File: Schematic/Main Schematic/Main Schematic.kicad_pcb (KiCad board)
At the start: 2 copper layers, 48 parts, among them IC1 DW01A-G, IC2 LM75AD,118, J1 Conn_01x24_Socket, J10 Conn_01x08_Pin, J3 Conn_01x24_Socket, J4 Conn_01x02_Male, J5 Conn_01x02_Male, J6 USB_B_Micro, J7 Conn_01x02_Pin, J8 Conn_01x24_Pin, J9 Conn_01x24_Pin, Q1 FS8205A, SW1 SW_Push, U1 HT75xx-1-SOT89, U2 MCP73831-2-OT, U3 CH340C, U4 M24C16-RMN6TP

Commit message: PCB UPDATE
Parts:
- moved TP7 109.6 mm to (106.4, 100.4)
- moved TP6 107.6 mm to (106.6, 105.0)
- moved J7 94.0 mm to (100.6, 107.3)
- moved J4 79.6 mm to (182.5, 79.5)
- moved U4 73.9 mm to (181.6, 130.4), turned to -90 degrees
- moved C7 73.0 mm to (126.8, 99.2), turned to -90 degrees
- moved J5 68.0 mm to (175.5, 79.5)
- moved U1 61.5 mm to (180.9, 94.0)
- moved J8 58.8 mm to (111.7, 119.4), turned to 90 degrees
- moved J9 56.8 mm to (111.7, 145.7), turned to 90 degrees
- moved J3 54.6 mm to (111.7, 124.5), turned to 90 degrees
- moved J1 53.5 mm to (111.7, 141.0), turned to 90 degrees
- moved IC2 52.8 mm to (159.0, 108.0), turned to -90 degrees
- moved TP2 50.6 mm to (132.0, 105.0)
- moved C2 50.1 mm to (175.9, 99.5), turned to -90 degrees
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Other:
- board outline added: 100 x 100 mm

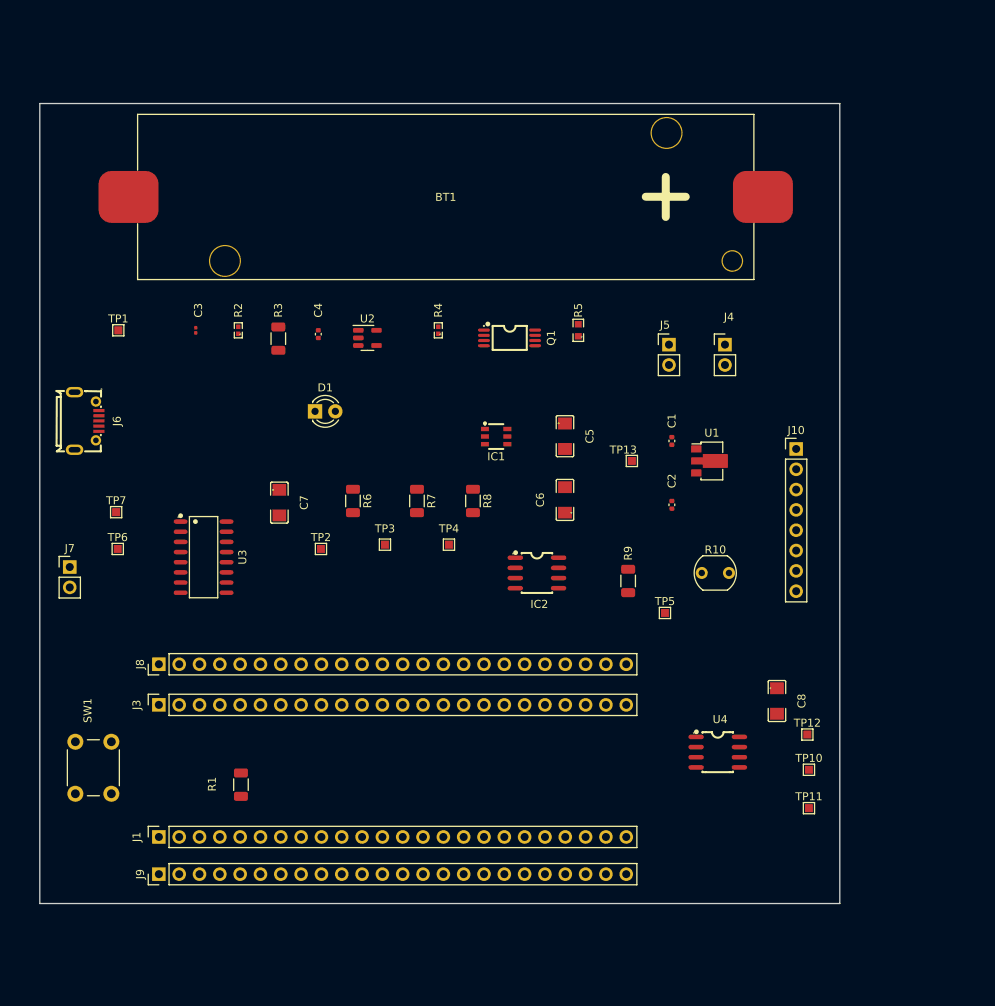
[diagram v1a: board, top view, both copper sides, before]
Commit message: traces done
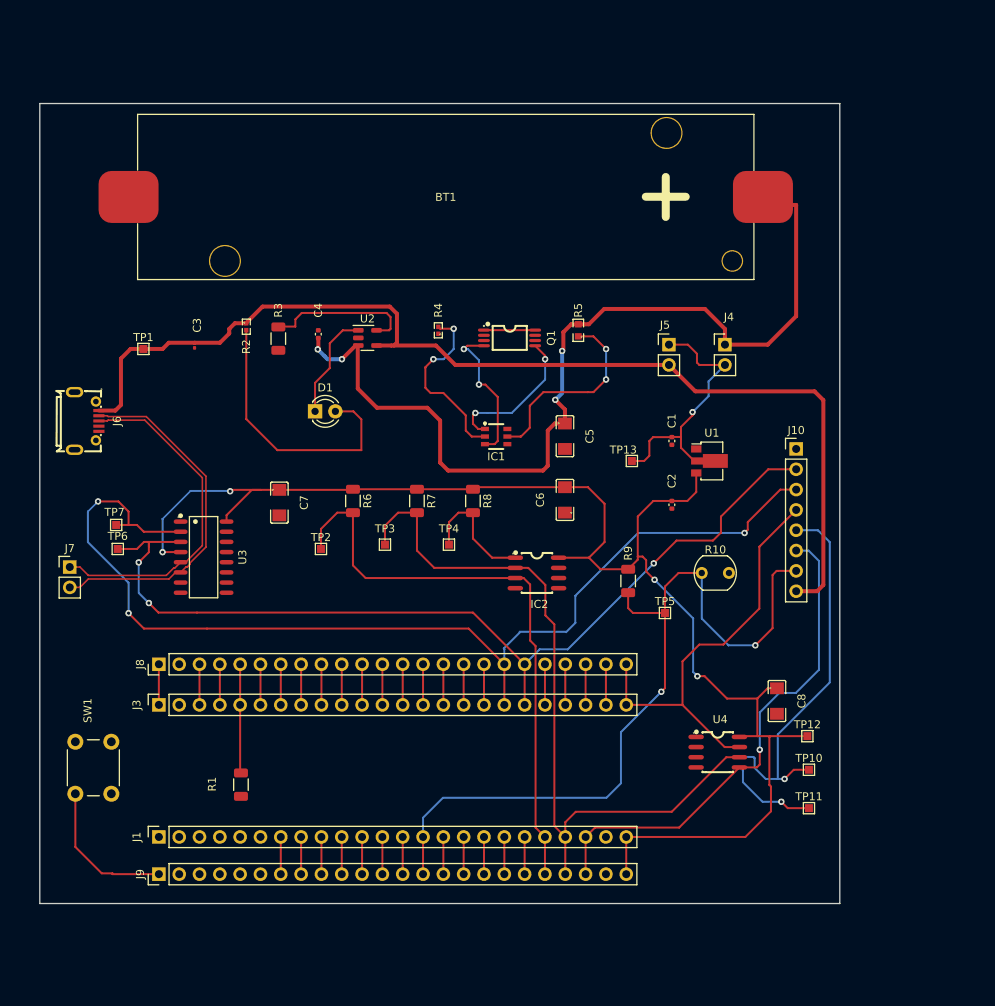
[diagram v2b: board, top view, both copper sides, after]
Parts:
- moved TP1 3.90 mm to (109.8, 80.0)
- moved C3 1.88 mm to (116.2, 79.5)
- moved TP7 1.60 mm to (106.4, 102.0)
- moved R2 1.10 mm to (122.7, 77.2), turned to -90 degrees
- moved TP12 0.20 mm to (192.8, 128.4)
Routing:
- net /3.3V: track 0.00 -> 192.1 mm, vias 0 -> 4
- net /SCL: track 0.00 -> 142.9 mm, vias 0 -> 1
- net /5V: track 0.00 -> 136.7 mm
- net /TXD: track 0.00 -> 135.1 mm, vias 0 -> 3
- net /RXD: track 0.00 -> 118.0 mm, vias 0 -> 3
- net /Power Unit/V1: track 0.00 -> 117.0 mm, vias 0 -> 4
- net /ADC: track 0.00 -> 99.4 mm, vias 0 -> 2
- net /SDL: track 0.00 -> 90.7 mm, vias 0 -> 2
- net /OS: track 0.00 -> 74.0 mm
- net /WRITE: track 0.00 -> 53.4 mm
- net /USB D-: track 0.00 -> 44.6 mm
- net /USB D+: track 0.00 -> 43.0 mm
- net Net-(D1-A): track 0.00 -> 34.6 mm
- net Net-(#FLG02-pwr): track 0.00 -> 32.6 mm, vias 0 -> 1
- net Net-(IC1-VCC): track 0.00 -> 24.8 mm, vias 0 -> 2
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
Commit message: updated the conn connections
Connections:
- J9 pad 2: /PF1 -> /PC13
- J9 pad 3: /PF0 -> /PC14
- J9 pad 5: /PC14 -> /PF0
- J9 pad 6: /PC13 -> /PF1
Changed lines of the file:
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@@
       (net 21 "/NRST") (pinfunction "Pin_1") (pintype "passive"))
     (pad "2" thru_hole oval (at 0 2.54 90) (size 1.7 1.7) (drill 1) (layers "*.Cu" "*.Mask")
-      (net 20 "/PF1") (pinfunction "Pin_2") (pintype "passive"))
+      (net 16 "/PC13") (pinfunction "Pin_2") (pintype "passive"))
     (pad "3" thru_hole oval (at 0 5.08 90) (size 1.7 1.7) (drill 1) (layers "*.Cu" "*.Mask")
-      (net 19 "/PF0") (pinfunction "Pin_3") (pintype "passive"))
+      (net 17 "/PC14") (pinfunction "Pin_3") (pintype "passive"))
     (pad "4" thru_hole oval (at 0 7.62 90) (size 1.7 1.7) (drill 1) (layers "*.Cu" "*.Mask")
       (net 18 "/PC15") (pinfunction "Pin_4") (pintype "passive"))
     (pad "5" thru_hole oval (at 0 10.16 90) (size 1.7 1.7) (drill 1) (layers "*.Cu" "*.Mask")
-      (net 17 "/PC14") (pinfunction "Pin_5") (pintype "passive"))
+      (net 19 "/PF0") (pinfunction "Pin_5") (pintype "passive"))
     (pad "6" thru_hole oval (at 0 12.7 90) (size 1.7 1.7) (drill 1) (layers "*.Cu" "*.Mask")
-      (net 16 "/PC13") (pinfunction "Pin_6") (pintype "passive"))
+      (net 20 "/PF1") (pinfunction "Pin_6") (pintype "passive"))
     (pad "7" thru_hole oval (at 0 15.24 90) (size 1.7 1.7) (drill 1) (layers "*.Cu" "*.Mask")
       (net 21 "/NRST") (pinfunction "Pin_7") (pintype "passive"))

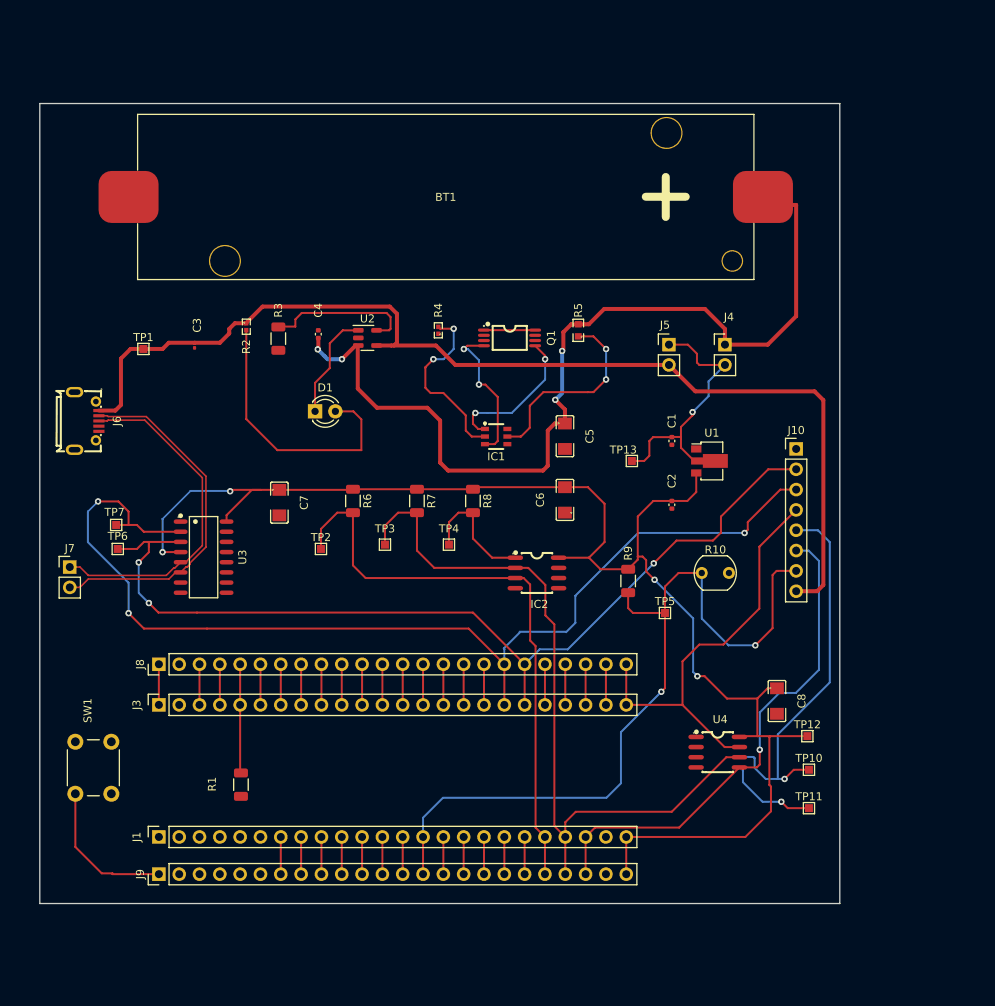
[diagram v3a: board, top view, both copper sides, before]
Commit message: traces done
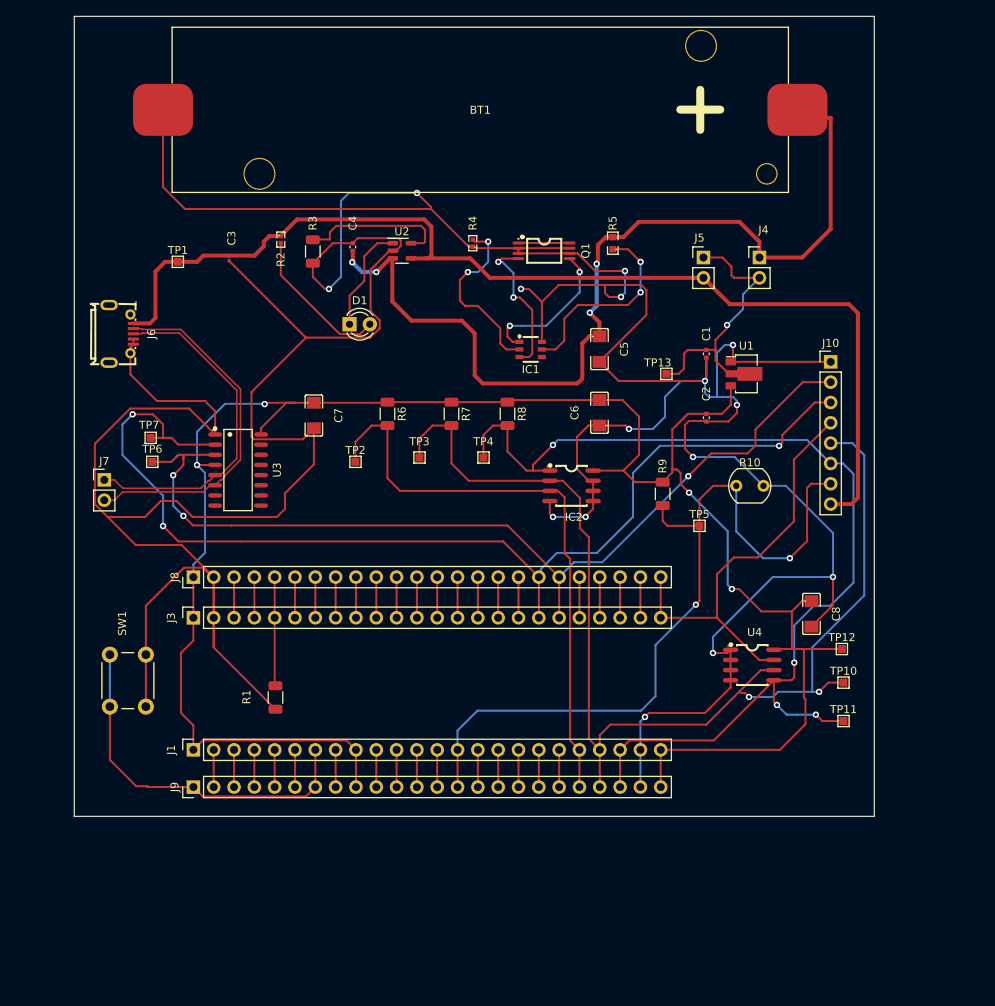
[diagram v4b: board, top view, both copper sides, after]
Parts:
- moved C4 11.7 mm to (136.0, 67.3)
- moved R4 11.7 mm to (151.0, 66.8)
- moved R5 11.7 mm to (168.5, 66.8)
- moved C7 11.7 mm to (131.1, 88.3)
- moved J1 11.7 mm to (116.1, 130.1)
- moved J7 11.7 mm to (104.9, 96.4)
- moved J9 11.7 mm to (116.1, 134.8)
- moved R1 11.7 mm to (126.3, 123.6)
- moved U3 11.7 mm to (121.6, 95.1)
- moved C2 11.7 mm to (180.2, 88.6)
- moved C3 11.7 mm to (120.5, 68.7)
- moved C8 11.7 mm to (193.3, 113.1)
- moved TP11 11.7 mm to (197.3, 126.5)
- moved TP12 11.7 mm to (197.1, 117.5)
- moved TP3 11.7 mm to (144.3, 93.6)
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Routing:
- net GND: track 0.00 -> 555.3 mm, vias 0 -> 15
- net /3.3V: track 192.1 -> 246.2 mm
- net /SDL: track 90.7 -> 131.9 mm, vias 2 -> 4
- net /NRST: track 23.2 -> 45.9 mm
- net Net-(D1-A): track 34.6 -> 18.7 mm
- net /PF1: track 0.00 -> 4.65 mm
- net /PF0: track 0.00 -> 4.65 mm
- net /PC15: track 0.00 -> 4.65 mm
- net /PC14: track 0.00 -> 4.65 mm
- net /PC13: track 0.00 -> 4.65 mm
- net /SCL: track 142.9 -> 145.8 mm, vias 1 -> 2

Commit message: I've added the local footprints and gerber files into the repo
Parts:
- BT1: footprint A_New_folder:18650_Holder_SMD -> Local_Footprints:18650_Holder_SMD
- C5, C6, C7, C8: footprint A_New_folder:C1206 -> Local_Footprints:C1206
- IC1: footprint A_New_folder:SOT-23-6_L2.9-W1.6-P0.95-LS2.8-BR -> Local_Footprints:SOT-23-6_L2.9-W1.6-P0.95-LS2.8-BR
- IC2, U4: footprint A_New_folder:SOIC-8_L5.0-W4.0-P1.27-LS6.0-BL -> Local_Footprints:SOIC-8_L5.0-W4.0-P1.27-LS6.0-BL
- J6: footprint A_New_folder:MICRO-USB-SMD_MICROXNJ -> Local_Footprints:MICRO-USB-SMD_MICROXNJ
- Q1: footprint A_New_folder:TSSOP-8_L4.4-W3.0-P0.65-LS6.4-BL-2 -> Local_Footprints:TSSOP-8_L4.4-W3.0-P0.65-LS6.4-BL-2
- R2, R4: footprint A_New_folder:R0402 -> Local_Footprints:R0402
- R5: footprint A_New_folder:R0603 -> Local_Footprints:C1206
- U3: footprint A_New_folder:SOP-16_L10.0-W3.9-P1.27-LS6.0-BL -> Local_Footprints:SOP-16_L10.0-W3.9-P1.27-LS6.0-BL
- moved J6 3.20 mm to (110.2, 78.6)
- moved TP1 3.07 mm to (117.1, 68.4)
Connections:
- TP6 pad 1: /RXD -> /TXD
- TP7 pad 1: /TXD -> /RXD
- U3 pad 2: /TXD -> /RXD
- U3 pad 3: /RXD -> /TXD
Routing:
- net GND: track 555.3 -> 545.1 mm
- net /5V: track 136.7 -> 133.8 mm
- net /USB D+: track 43.0 -> 40.5 mm
- net /USB D-: track 44.6 -> 42.1 mm
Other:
- board text added: "TEAM 26 ZWIVHUYA NDOU SIVUYILE NOSE TALIFHANI NEMAANGANI"
